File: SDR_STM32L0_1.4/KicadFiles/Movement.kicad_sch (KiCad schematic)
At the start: 22 parts, among them U1 MAX-8C-0-10, U6 BMI323, U7 BMP390

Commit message: begin routing
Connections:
- net Earth is gone; now on net GND: BT1.2 (-)
- net GPS: now also L1.2; no longer L1.1
- net GPS_RST: now also R17.2; no longer R17.1
- net at C20.1, R16.1: now also L1.1; no longer L1.2
- net at U1.9 (~{RESET}): now also R17.1; no longer R17.2
- net BP_INT renamed BP_INT****
- net IMU_INPUT renamed IMU_INPUT***
- net IMU_OUTPUT renamed IMU_OUTPUT***
- net USART2_RX renamed USART1_RX
- net USART2_TX renamed USART1_TX
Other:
- moved on the sheet: R17

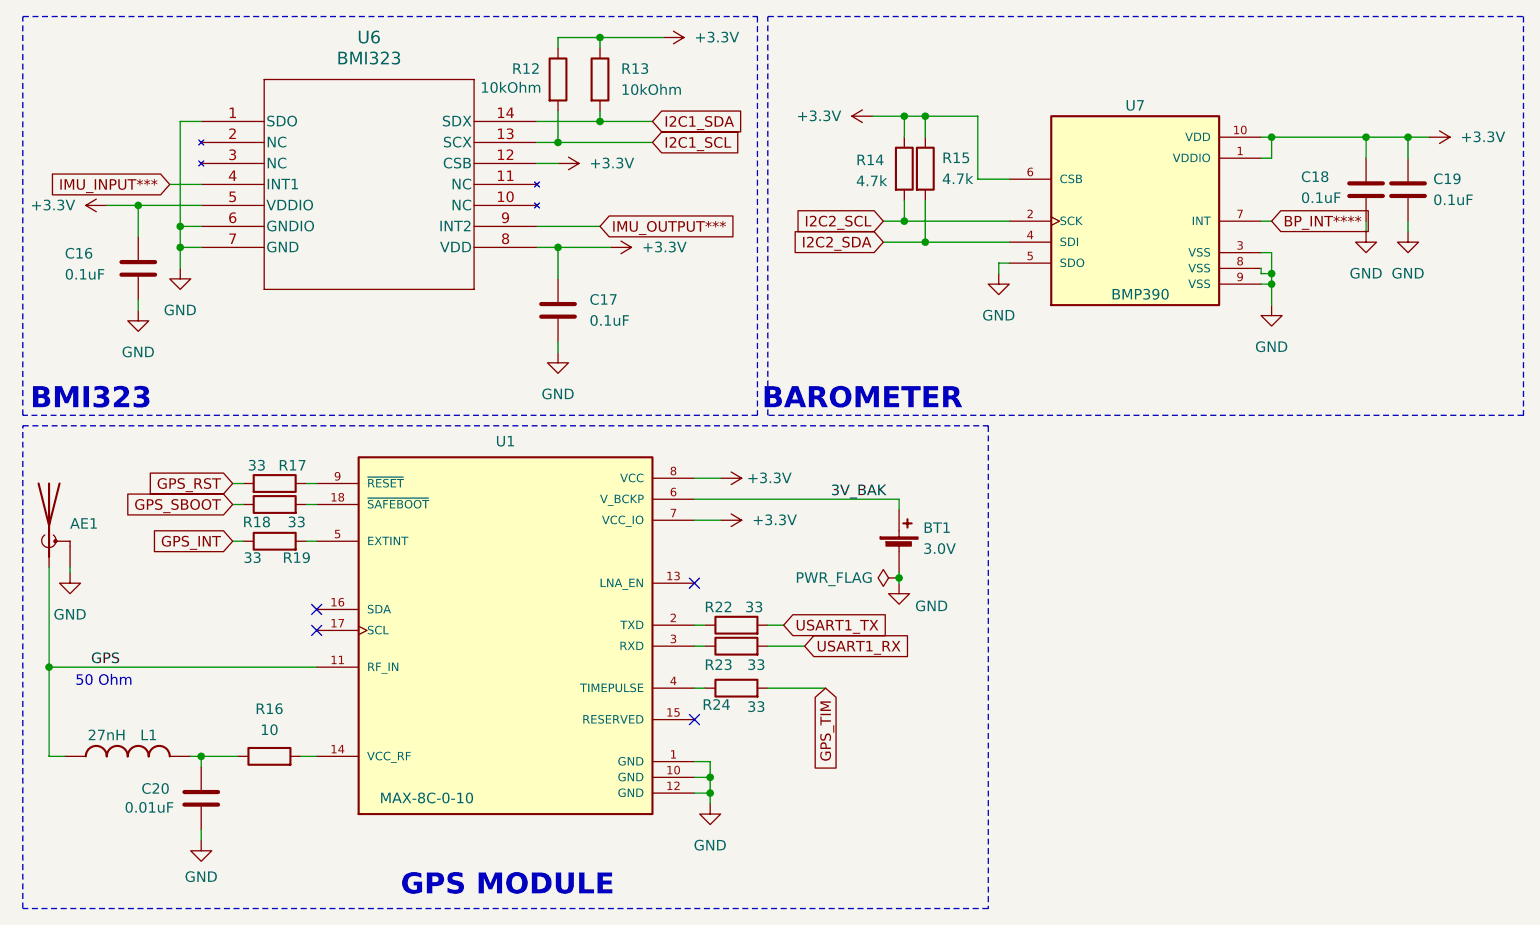
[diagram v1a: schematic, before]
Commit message: Upgrade
Changed a few peripherals (less ports, +/- on ports, switched jumpers, switched pinouts), and made new shematic
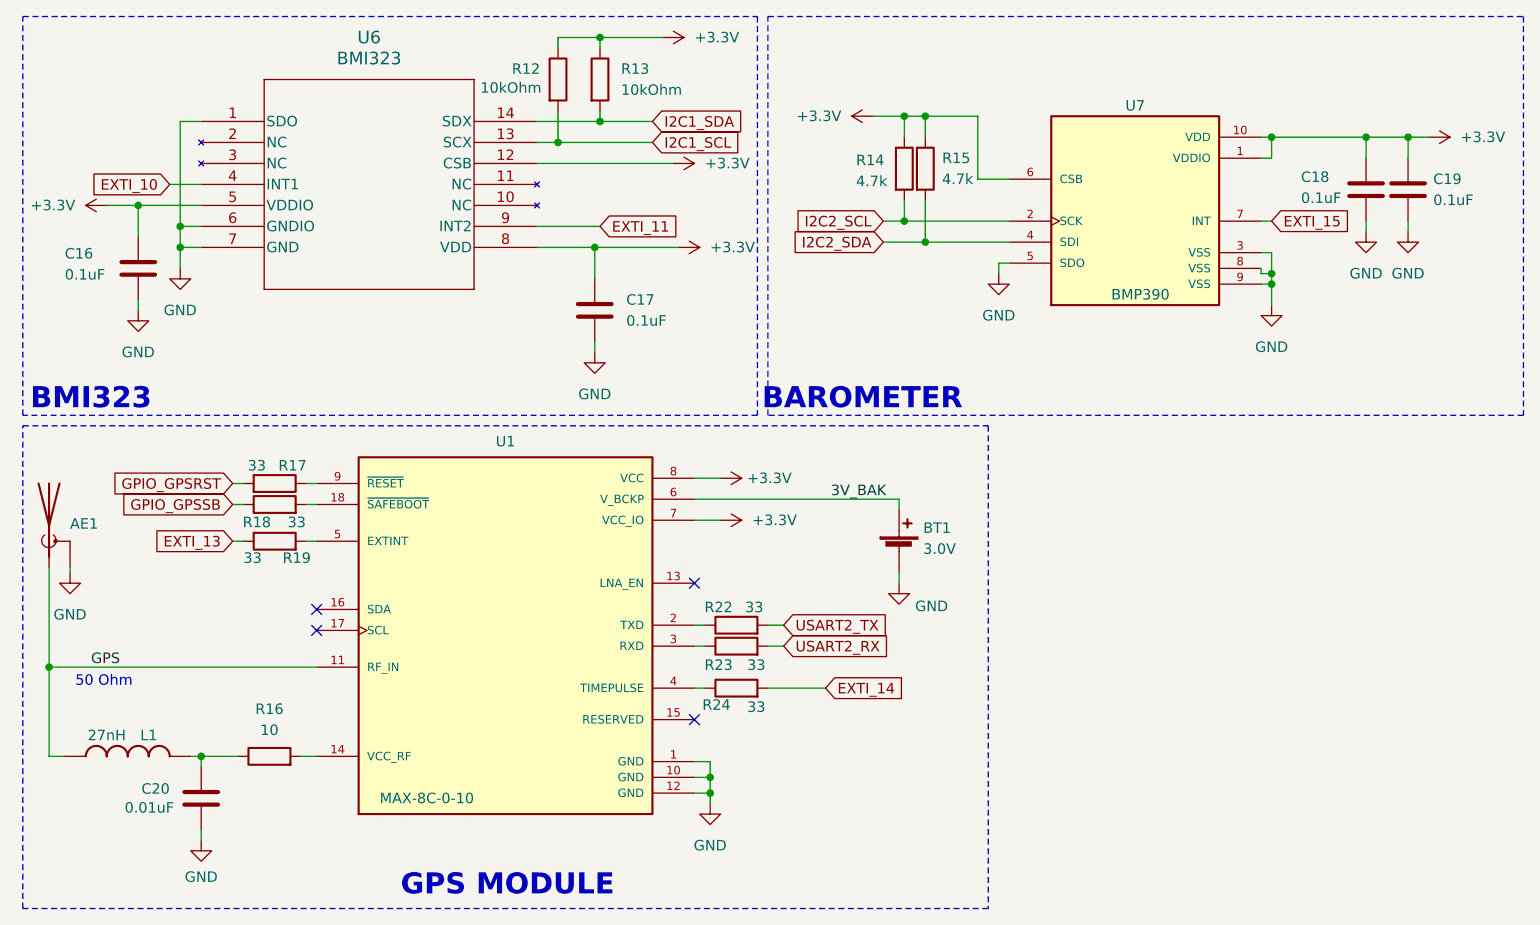
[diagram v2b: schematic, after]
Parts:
- AE1: footprint FlightComputer:73412-0110 -> FCMac:73412-0110
- BT1: footprint FlightComputer:MS621FE-FL11E -> FCMac:MS621FE-FL11E
- C16, C17, C18, C19: footprint Capacitor_SMD:C_0402_1005Metric -> Capacitor_SMD:C_0603_1608Metric
- C20: footprint Capacitor_SMD:C_0201_0603Metric -> Capacitor_SMD:C_0603_1608Metric
- L1: footprint FlightComputer:L-07C27NJV6T -> FCMac:L-07C27NJV6T
- R12, R13, R14, R15, R16: footprint Resistor_SMD:R_0402_1005Metric -> Resistor_SMD:R_0603_1608Metric
- R17, R18, R19, R22, R23, R24: footprint Resistor_SMD:R_0612_1632Metric -> Resistor_SMD:R_0603_1608Metric
- U1: footprint FlightComputer:MAX-8C-0 -> FCMac:MAX-8C-0
- U6: footprint FlightComputer:BMI323 -> FCMac:BMI323
- U7: footprint FlightComputer:BMP390 -> FCMac:BMP390
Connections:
- net BP_INT**** renamed EXTI_15
- net GPS_INT renamed EXTI_13
- net GPS_RST renamed GPIO_GPSRST
- net GPS_SBOOT renamed GPIO_GPSSB
- net GPS_TIM renamed EXTI_14
- net IMU_INPUT*** renamed EXTI_10
- net IMU_OUTPUT*** renamed EXTI_11
- net USART1_RX renamed USART2_RX
- net USART1_TX renamed USART2_TX
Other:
- moved on the sheet: C17
